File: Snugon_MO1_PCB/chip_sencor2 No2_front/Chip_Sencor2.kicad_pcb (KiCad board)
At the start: 2 copper layers, 30 x 61.8 mm, 8 parts, among them J4 Conn_01x8_Pin + 2, SW12 RotaryEncoder, SW2 SW_PUSH, SW3 SW_PUSH, SW4 SW_PUSH, SW5 SW_PUSH, SW6 SW_PUSH

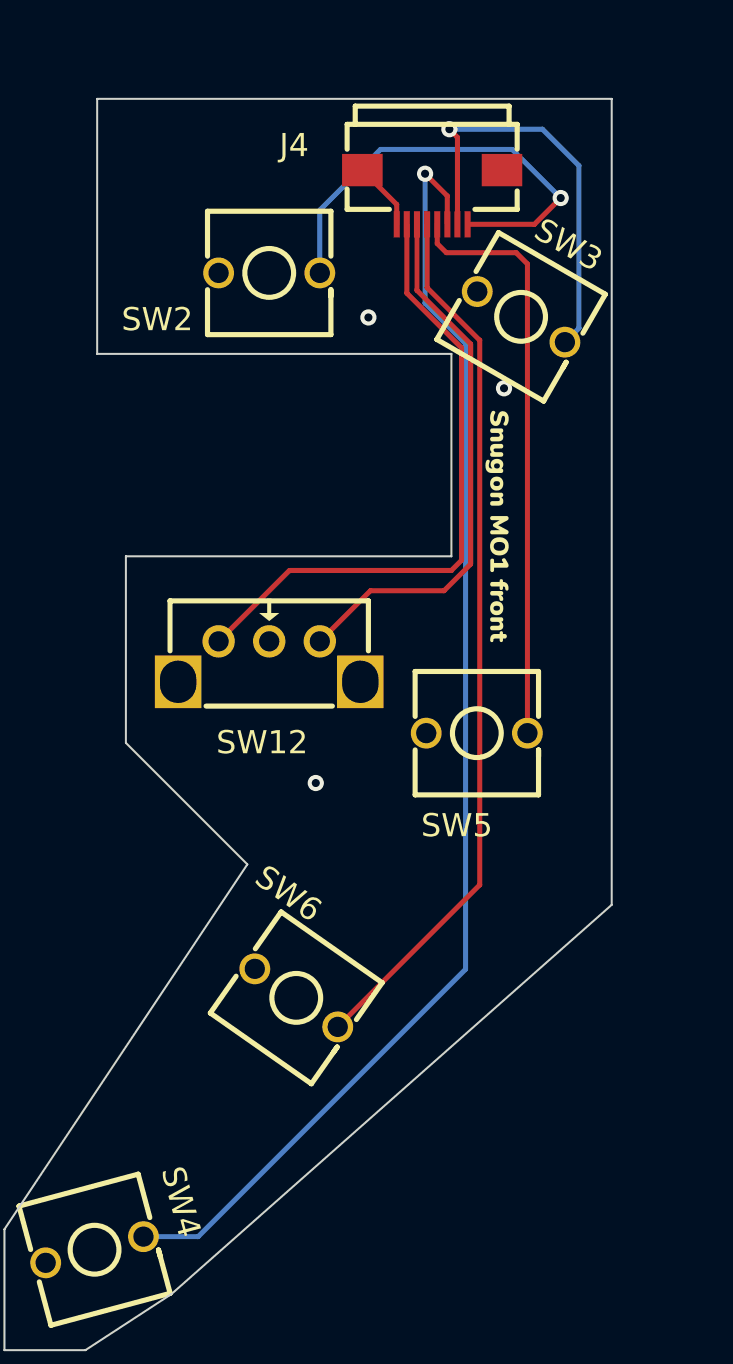
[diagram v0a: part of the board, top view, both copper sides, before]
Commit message: スイッチとエンコーダーはPCBAしない
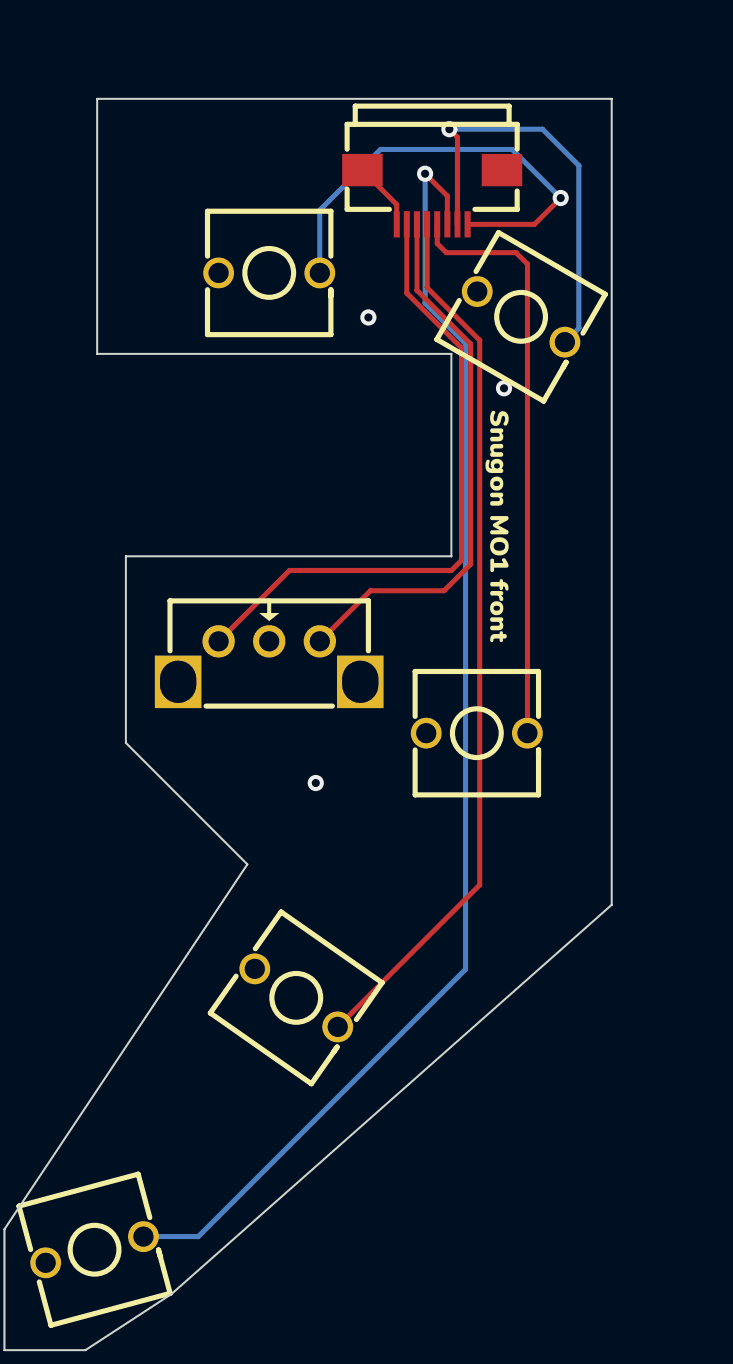
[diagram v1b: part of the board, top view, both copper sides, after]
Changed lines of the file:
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@@
   (footprint "0:SW-TH_L6.2-W6.2-P5.00" (layer "F.Cu")
     (at 126.543 80.77 -30)
-    (property "LCSC" "C400268")
-    (property "Sheetfile" "Chip_Sencor2.kicad_sch")
-    (property "Sheetname" "")
-    (attr through_hole)
-    (fp_text reference "SW3" (at 2.02258 -4.250788 150) (layer "F.SilkS")
+    (property "LCSC" "")
+    (property "Sheetfile" "Chip_Sencor2.kicad_sch")
+    (property "Sheetname" "")
+    (attr through_hole)
+    (fp_text reference "SW3" (at 2.02258 -4.250788 150) (layer "F.SilkS") hide
         (effects (font (size 1.143 1.143) (thickness 0.152)) (justify right))
     )
@@
   (footprint "0:SW-TH_CEN971112R02" (layer "F.Cu")
     (at 114.1 97.8 180)
-    (property "LCSC" "C400278")
+    (property "LCSC" "")
     (property "Sheetfile" "Chip_Sencor2.kicad_sch")
     (property "Sheetname" "")
@@
     (property "ki_keywords" "rotary switch encoder")
     (attr through_hole)
-    (fp_text reference "SW12" (at -1.92 -4) (layer "F.SilkS")
+    (fp_text reference "SW12" (at -1.92 -4) (layer "F.SilkS") hide
         (effects (font (size 1.143 1.143) (thickness 0.152)) (justify right))
     )
@@
   (footprint "0:SW-TH_L6.2-W6.2-P5.00" (layer "F.Cu")
     (at 115.436 114.414 -35)
-    (property "LCSC" "C400268")
-    (property "Sheetfile" "Chip_Sencor2.kicad_sch")
-    (property "Sheetname" "")
-    (attr through_hole)
-    (fp_text reference "SW6" (at -1.5 -4 145) (layer "F.SilkS")
+    (property "LCSC" "")
+    (property "Sheetfile" "Chip_Sencor2.kicad_sch")
+    (property "Sheetname" "")
+    (attr through_hole)
+    (fp_text reference "SW6" (at -1.5 -4 145) (layer "F.SilkS") hide
         (effects (font (size 1.143 1.143) (thickness 0.152)) (justify right))
     )
@@
     (property "ki_keywords" "connector")
     (attr smd)
-    (fp_text reference "J4" (at -7.55 -2.56) (layer "F.SilkS")
+    (fp_text reference "J4" (at -7.55 -2.56) (layer "F.SilkS") hide
         (effects (font (size 1.143 1.143) (thickness 0.152)) (justify left))
     )
@@
   (footprint "0:SW-TH_L6.2-W6.2-P5.00" (layer "F.Cu")
     (at 124.357 101.337)
-    (property "LCSC" "C400268")
-    (property "Sheetfile" "Chip_Sencor2.kicad_sch")
-    (property "Sheetname" "")
-    (attr through_hole)
-    (fp_text reference "SW5" (at -2.757 4.563) (layer "F.SilkS")
+    (property "LCSC" "")
+    (property "Sheetfile" "Chip_Sencor2.kicad_sch")
+    (property "Sheetname" "")
+    (attr through_hole)
+    (fp_text reference "SW5" (at -2.757 4.563) (layer "F.SilkS") hide
         (effects (font (size 1.143 1.143) (thickness 0.152)) (justify left))
     )
@@
   (footprint "0:SW-TH_L6.2-W6.2-P5.00" (layer "F.Cu")
     (at 114.1 78.6)
-    (property "LCSC" "C400268")
-    (property "Sheetfile" "Chip_Sencor2.kicad_sch")
-    (property "Sheetname" "")
-    (attr through_hole)
-    (fp_text reference "SW2" (at -7.3 2.3 180) (layer "F.SilkS")
+    (property "LCSC" "")
+    (property "Sheetfile" "Chip_Sencor2.kicad_sch")
+    (property "Sheetname" "")
+    (attr through_hole)
+    (fp_text reference "SW2" (at -7.3 2.3 180) (layer "F.SilkS") hide
         (effects (font (size 1.143 1.143) (thickness 0.152)) (justify left))
     )
@@
   (footprint "0:SW-TH_L6.2-W6.2-P5.00" (layer "F.Cu")
     (at 105.472 126.856 15)
-    (property "LCSC" "C400268")
-    (property "Sheetfile" "Chip_Sencor2.kicad_sch")
-    (property "Sheetname" "")
-    (attr through_hole)
-    (fp_text reference "SW4" (at 4.736683 0.590049 105) (layer "F.SilkS")
-        (effects (font (size 1.143 1.143) (thickness 0.152)) (justify right))
-    )
+    (property "LCSC" "")
+    (property "Sheetfile" "Chip_Sencor2.kicad_sch")
+    (property "Sheetname" "")
+    (attr through_hole)
+    (fp_text reference "SW4" (at 4.736683 0.590049 105) (layer "F.SilkS") hide
+        (effects (font (size 1.143 1.143) (thickness 0.152)) (justify right))
+    )

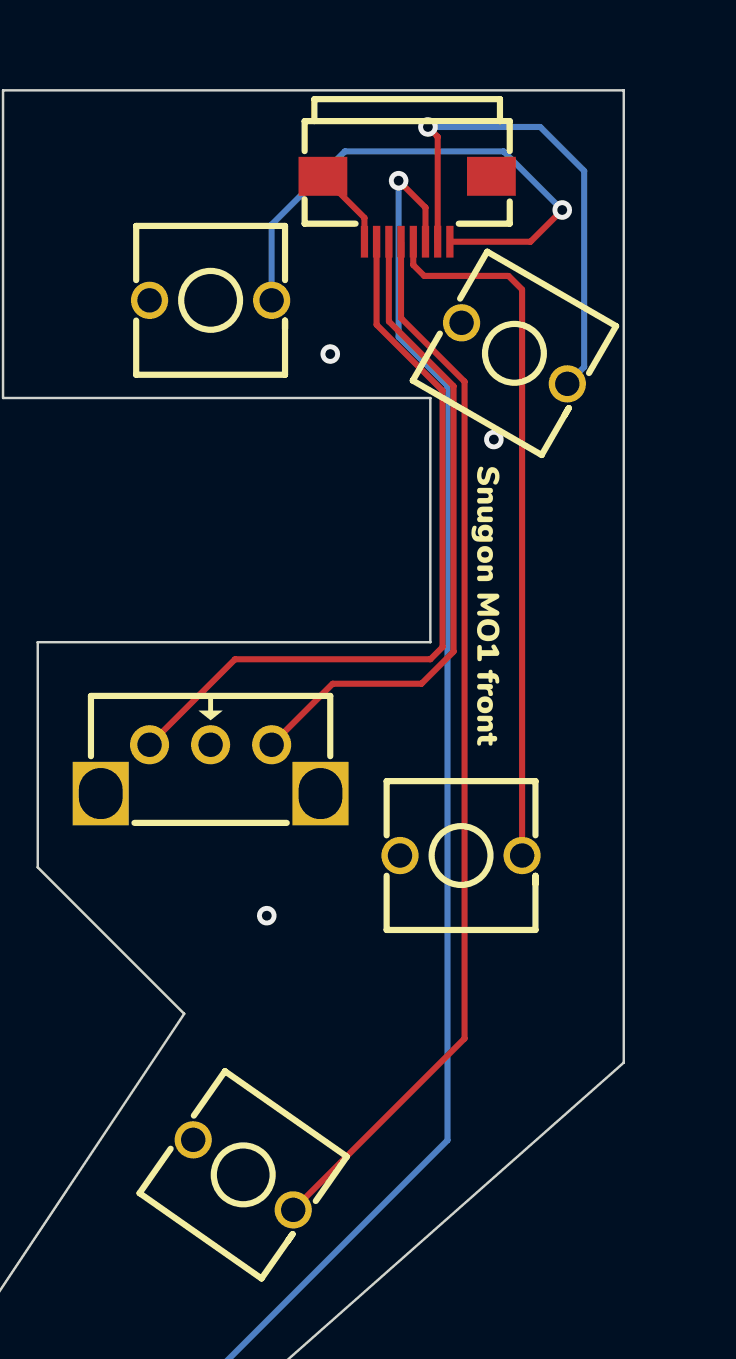
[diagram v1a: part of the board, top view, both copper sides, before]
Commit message: エンコーダの配線修正
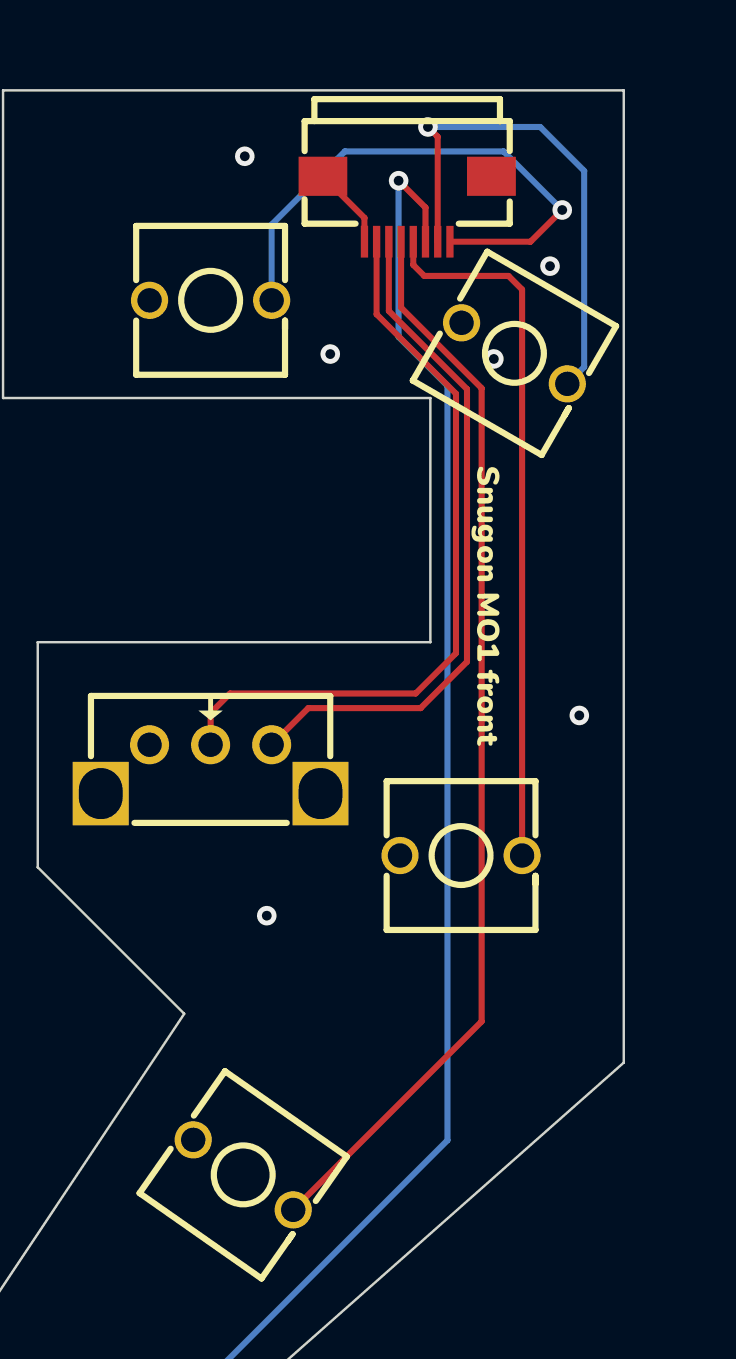
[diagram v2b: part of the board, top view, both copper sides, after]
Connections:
- SW12 pad 2: GND -> RE0B_F
- SW12 pad 3: RE0B_F -> GND
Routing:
- net RE0A_F: track 26.9 -> 27.9 mm
- net RE0B_F: track 31.4 -> 30.6 mm
- net SW6_F: track 43.6 -> 44.2 mm
- net GND: vias 3 -> 6
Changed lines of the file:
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@@
       (net 7 "RE0A_F") (pinfunction "A") (pintype "passive"))
     (pad "2" thru_hole circle (at 0 1 180) (size 1.6 1.6) (drill 1) (layers "*.Cu" "*.Paste" "*.Mask")
-      (net 1 "GND") (pinfunction "2") (pintype "passive"))
+      (net 8 "RE0B_F") (pinfunction "2") (pintype "passive"))
     (pad "3" thru_hole circle (at 2.5 1 180) (size 1.6 1.6) (drill 1) (layers "*.Cu" "*.Paste" "*.Mask")
-      (net 8 "RE0B_F") (pinfunction "3") (pintype "passive"))
+      (net 1 "GND") (pinfunction "3") (pintype "passive"))
     (pad "4" thru_hole rect (at -4.5 -1 180) (size 2.3 2.6) (drill oval 1.8 2.1) (layers "*.Cu" "*.Paste" "*.Mask"))
     (pad "5" thru_hole rect (at 4.5 -1 180) (size 2.3 2.6) (drill oval 1.8 2.1) (layers "*.Cu" "*.Paste" "*.Mask"))
@@
   (segment (start 120.4 75.22) (end 118.7 73.52) (width 0.25) (layer "F.Cu") (net 1))
   (segment (start 120.4 76.2) (end 120.4 75.22) (width 0.25) (layer "F.Cu") (net 1))
+  (via (at 128 77.2) (size 0.8) (drill 0.4) (layers "F.Cu" "B.Cu") (free) (net 1))
+  (via (at 129.2 95.6) (size 0.8) (drill 0.4) (layers "F.Cu" "B.Cu") (free) (net 1))
   (via (at 119 80.8) (size 0.8) (drill 0.4) (layers "F.Cu" "B.Cu") (free) (net 1))
-  (via (at 125.7 84.3) (size 0.8) (drill 0.4) (layers "F.Cu" "B.Cu") (free) (net 1))
+  (via (at 125.7 81) (size 0.8) (drill 0.4) (layers "F.Cu" "B.Cu") (free) (net 1))
   (via (at 116.4 103.8) (size 0.8) (drill 0.4) (layers "F.Cu" "B.Cu") (free) (net 1))
+  (via (at 115.5 72.7) (size 0.8) (drill 0.4) (layers "F.Cu" "B.Cu") (free) (net 1))
   (segment (start 123.4 76.2) (end 123.4 71.9) (width 0.25) (layer "F.Cu") (net 2))
   (segment (start 123.4 71.9) (end 123 71.5) (width 0.25) (layer "F.Cu") (net 2))
@@
   (segment (start 126.857 78.157) (end 126.857 101.337) (width 0.25) (layer "F.Cu") (net 5))
   (segment (start 122.4 76.2) (end 122.4 77.15) (width 0.25) (layer "F.Cu") (net 5))
-  (segment (start 124.5 108.831821) (end 117.48388 115.847941) (width 0.25) (layer "F.Cu") (net 6))
-  (segment (start 121.9 79.327208) (end 124.5 81.927208) (width 0.25) (layer "F.Cu") (net 6))
-  (segment (start 124.5 81.927208) (end 124.5 108.831821) (width 0.25) (layer "F.Cu") (net 6))
-  (segment (start 121.9 76.2) (end 121.9 79.327208) (width 0.25) (layer "F.Cu") (net 6))
-  (segment (start 119.1 94.3) (end 116.6 96.8) (width 0.25) (layer "F.Cu") (net 7))
-  (segment (start 122.736396 94.3) (end 119.1 94.3) (width 0.25) (layer "F.Cu") (net 7))
-  (segment (start 124.05 92.986396) (end 122.736396 94.3) (width 0.25) (layer "F.Cu") (net 7))
-  (segment (start 121.4 79.463604) (end 124.05 82.113604) (width 0.25) (layer "F.Cu") (net 7))
-  (segment (start 121.4 76.2) (end 121.4 79.463604) (width 0.25) (layer "F.Cu") (net 7))
-  (segment (start 124.05 82.113604) (end 124.05 92.986396) (width 0.25) (layer "F.Cu") (net 7))
-  (segment (start 120.898 79.598) (end 123.6 82.3) (width 0.25) (layer "F.Cu") (net 8))
-  (segment (start 123.6 92.8) (end 123.1 93.3) (width 0.25) (layer "F.Cu") (net 8))
-  (segment (start 120.898 76.198) (end 120.898 79.598) (width 0.25) (layer "F.Cu") (net 8))
-  (segment (start 123.1 93.3) (end 115.1 93.3) (width 0.25) (layer "F.Cu") (net 8))
-  (segment (start 123.6 82.3) (end 123.6 92.8) (width 0.25) (layer "F.Cu") (net 8))
-  (segment (start 115.1 93.3) (end 111.6 96.8) (width 0.25) (layer "F.Cu") (net 8))
+  (segment (start 125.2 82.2) (end 125.2 108.131821) (width 0.25) (layer "F.Cu") (net 6))
+  (segment (start 121.9 76.2) (end 121.9 78.9) (width 0.25) (layer "F.Cu") (net 6))
+  (segment (start 125.2 108.131821) (end 117.48388 115.847941) (width 0.25) (layer "F.Cu") (net 6))
+  (segment (start 121.9 78.9) (end 125.2 82.2) (width 0.25) (layer "F.Cu") (net 6))
+  (segment (start 121.4 76.2) (end 121.4 79.036396) (width 0.25) (layer "F.Cu") (net 7))
+  (segment (start 118.1 95.3) (end 116.6 96.8) (width 0.25) (layer "F.Cu") (net 7))
+  (segment (start 124.6 93.4) (end 122.7 95.3) (width 0.25) (layer "F.Cu") (net 7))
+  (segment (start 122.7 95.3) (end 118.1 95.3) (width 0.25) (layer "F.Cu") (net 7))
+  (segment (start 124.6 82.236396) (end 124.6 93.4) (width 0.25) (layer "F.Cu") (net 7))
+  (segment (start 121.4 79.036396) (end 124.6 82.236396) (width 0.25) (layer "F.Cu") (net 7))
+  (segment (start 114.1 95.5) (end 114.1 96.8) (width 0.25) (layer "F.Cu") (net 8))
+  (segment (start 124.15 93.05) (end 122.5 94.7) (width 0.25) (layer "F.Cu") (net 8))
+  (segment (start 114.9 94.7) (end 114.1 95.5) (width 0.25) (layer "F.Cu") (net 8))
+  (segment (start 120.898 79.170792) (end 124.15 82.422792) (width 0.25) (layer "F.Cu") (net 8))
+  (segment (start 120.898 76.198) (end 120.898 79.170792) (width 0.25) (layer "F.Cu") (net 8))
+  (segment (start 124.15 82.422792) (end 124.15 93.05) (width 0.25) (layer "F.Cu") (net 8))
+  (segment (start 122.5 94.7) (end 114.9 94.7) (width 0.25) (layer "F.Cu") (net 8))
   (zone (net 1) (net_name "GND") (layer "F.Cu") (hatch edge 0.5)
     (connect_pads (clearance 0.5))
